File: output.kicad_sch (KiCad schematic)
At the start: 74 parts

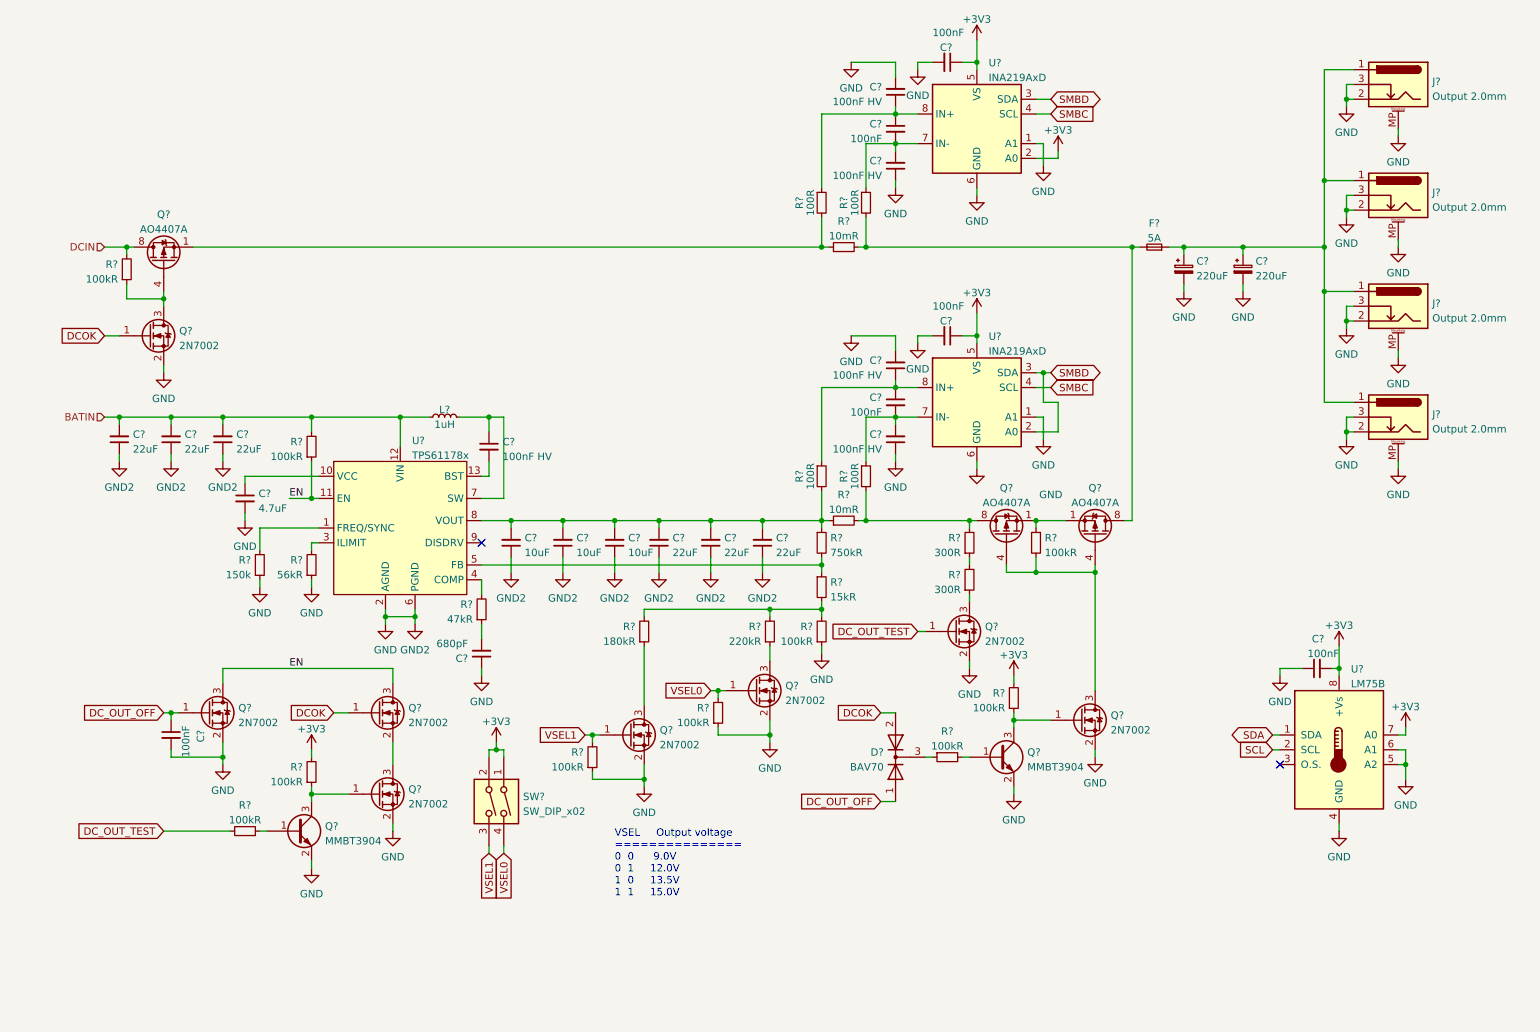
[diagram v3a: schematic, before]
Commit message: Add individually switchable outputs
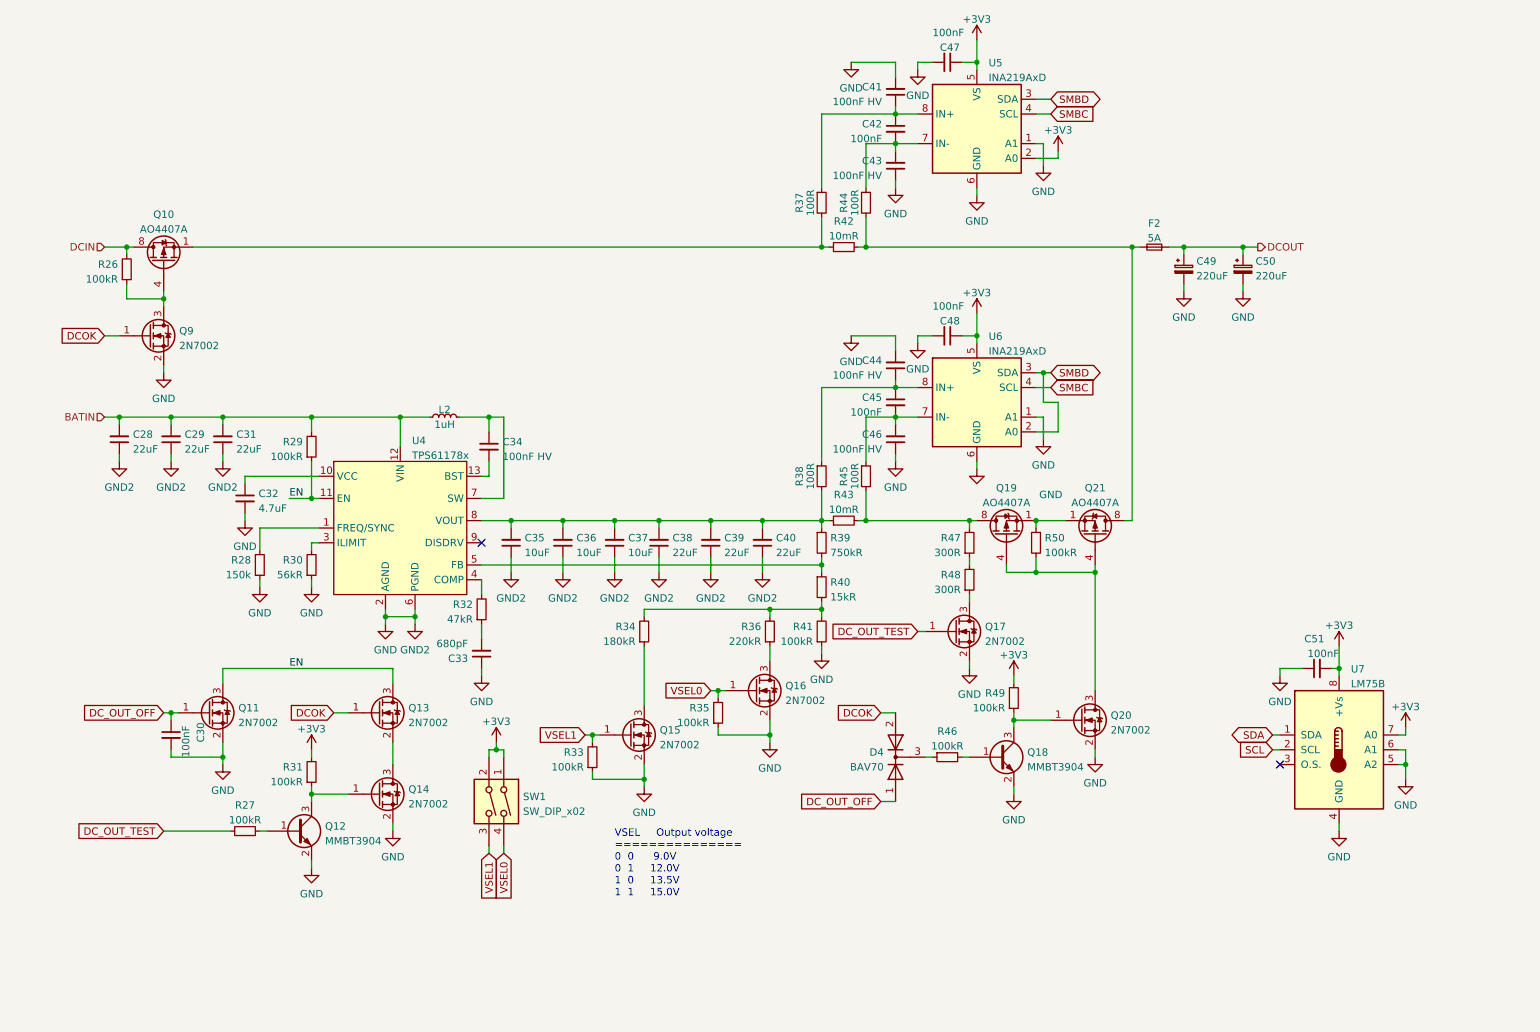
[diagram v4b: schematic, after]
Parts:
- removed J? (x4): Output 2.0mm, Connector_BarrelJack_LCSC:BarrelJack_2.0mm_DC-044B, symbol Connector:Barrel_Jack_Switch_MountingPin
- gave numbers to parts that had none: 70
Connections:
- net DCOUT: now reaches C49.1, C50.1, F2.1

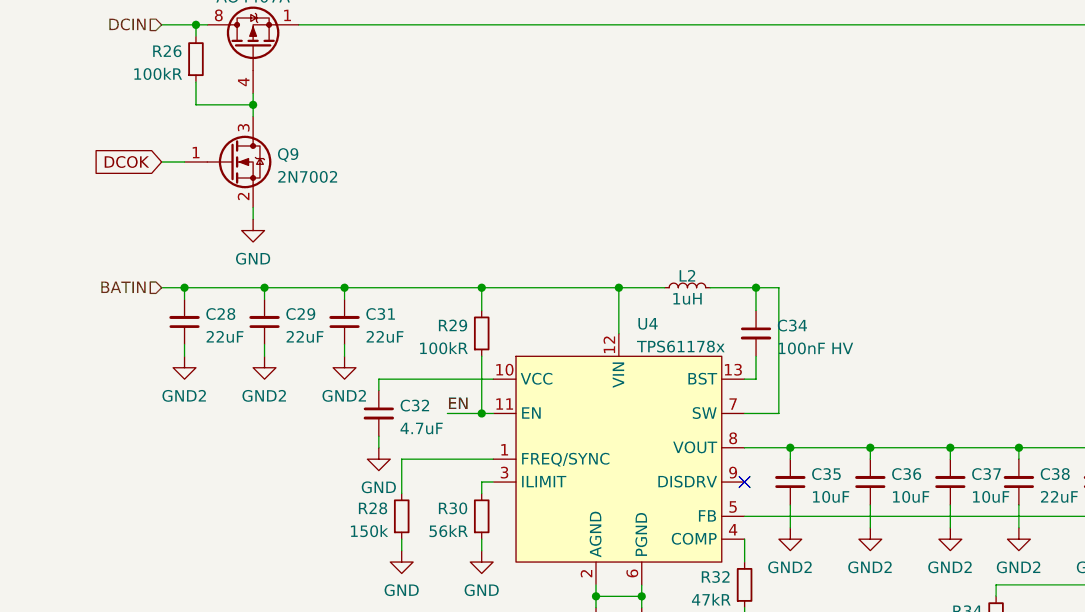
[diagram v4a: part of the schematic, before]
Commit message: Finish step-up component placement and partial layout
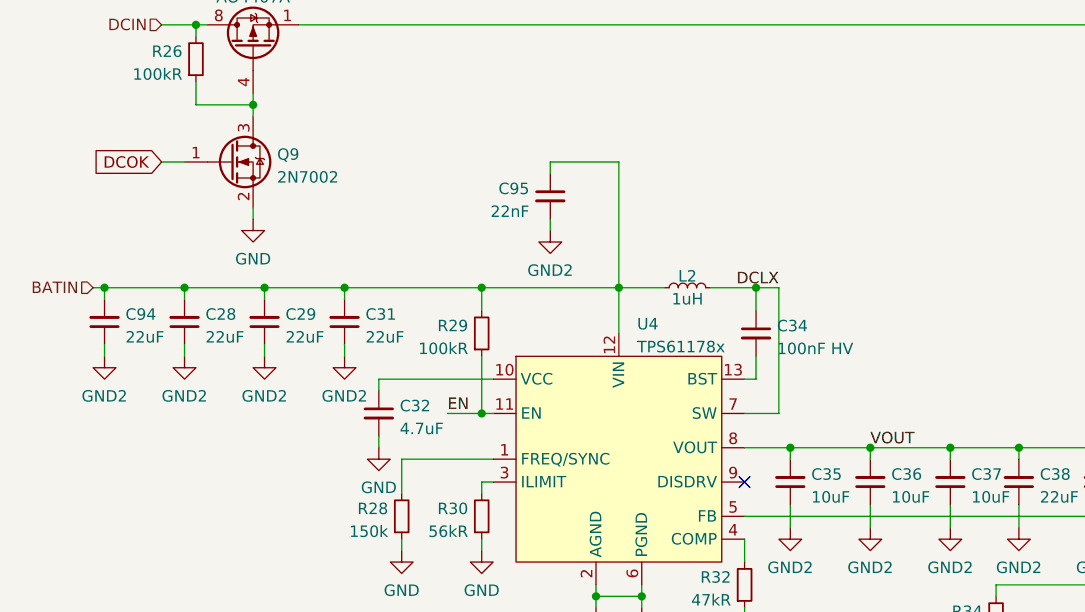
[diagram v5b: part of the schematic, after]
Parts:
- added C94: 22uF, Capacitor_SMD:C_0805_2012Metric, symbol Device:C_Small
- added C95: 22nF, Capacitor_SMD:C_0402_1005Metric, symbol Device:C_Small
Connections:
- net BATIN: now also C94.2, C95.1
- net GND: now also C94.1, C95.2
- net VOUT: now reaches C35.2, C36.2, C37.2, C38.2, C39.2, C40.2, R38.2, R39.1, R43.1, U4.8 (VOUT)
- net DCLX: now reaches C34.1, L2.2, U4.7 (SW)
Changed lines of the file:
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@@
   (junction (at 161.29 104.14) (diameter 0) (color 0 0 0 0)
+  )
+  (junction (at 31.75 86.36) (diameter 0) (color 0 0 0 0)
   )
   (junction (at 58.42 144.78) (diameter 0) (color 0 0 0 0)
@@
     (stroke (width 0) (type default) (color 0 0 0 0))
   )
+  (wire (pts (xy 31.75 86.36) (xy 40.64 86.36))
+    (stroke (width 0) (type default) (color 0 0 0 0))
+  )
   (wire (pts (xy 168.91 57.15) (xy 214.63 57.15))
     (stroke (width 0) (type default) (color 0 0 0 0))
@@
     (stroke (width 0) (type default) (color 0 0 0 0))
   )
+  (wire (pts (xy 81.28 72.39) (xy 81.28 73.66))
+    (stroke (width 0) (type default) (color 0 0 0 0))
+  )
   (wire (pts (xy 173.99 39.37) (xy 173.99 40.64))
     (stroke (width 0) (type default) (color 0 0 0 0))
@@
     (stroke (width 0) (type default) (color 0 0 0 0))
   )
-  (wire (pts (xy 38.1 86.36) (xy 40.64 86.36))
+  (wire (pts (xy 30.48 86.36) (xy 31.75 86.36))
     (stroke (width 0) (type default) (color 0 0 0 0))
   )
@@
     (stroke (width 0) (type default) (color 0 0 0 0))
   )
+  (wire (pts (xy 31.75 92.71) (xy 31.75 93.98))
+    (stroke (width 0) (type default) (color 0 0 0 0))
+  )
+  (wire (pts (xy 88.9 72.39) (xy 81.28 72.39))
+    (stroke (width 0) (type default) (color 0 0 0 0))
+  )
   (wire (pts (xy 48.26 77.47) (xy 48.26 78.74))
     (stroke (width 0) (type default) (color 0 0 0 0))
@@
     (stroke (width 0) (type default) (color 0 0 0 0))
   )
+  (wire (pts (xy 31.75 86.36) (xy 31.75 87.63))
+    (stroke (width 0) (type default) (color 0 0 0 0))
+  )
   (wire (pts (xy 62.23 96.52) (xy 62.23 97.79))
     (stroke (width 0) (type default) (color 0 0 0 0))
@@
     (stroke (width 0) (type default) (color 0 0 0 0))
   )
+  (wire (pts (xy 88.9 86.36) (xy 88.9 72.39))
+    (stroke (width 0) (type default) (color 0 0 0 0))
+  )
   (wire (pts (xy 186.69 116.84) (xy 186.69 118.11))
     (stroke (width 0) (type default) (color 0 0 0 0))
@@
   )
   (wire (pts (xy 194.31 138.43) (xy 194.31 139.7))
+    (stroke (width 0) (type default) (color 0 0 0 0))
+  )
+  (wire (pts (xy 81.28 78.74) (xy 81.28 80.01))
     (stroke (width 0) (type default) (color 0 0 0 0))
   )
@@
     (effects (font (size 1.27 1.27)) (justify left bottom))
   )
+  (label "DCLX" (at 106.68 86.36 180)
+    (effects (font (size 1.27 1.27)) (justify right bottom))
+  )
   (label "EN" (at 69.85 129.54 0)
+    (effects (font (size 1.27 1.27)) (justify left bottom))
+  )
+  (label "VOUT" (at 116.84 104.14 0)
     (effects (font (size 1.27 1.27)) (justify left bottom))
   )
@@
     (effects (font (size 1.27 1.27)) (justify left))
   )
-  (hierarchical_label "BATIN" (shape input) (at 38.1 86.36 180)
+  (hierarchical_label "BATIN" (shape input) (at 30.48 86.36 180)
     (effects (font (size 1.27 1.27)) (justify right))
   )
@@
     )
     (property "LCSC" "C25767" (id 4) (at 152.4 123.19 0)
+      (effects (font (size 1.27 1.27)) hide)
+    )
+    (pin "1")
+    (pin "2")
+  )
+  (symbol (lib_id "Device:C_Small") (at 81.28 76.2 0) (mirror y) (unit 1)
+    (in_bom yes) (on_board yes)
+    (property "Reference" "C95" (id 0) (at 78.9559 75.3716 0)
+      (effects (font (size 1.27 1.27)) (justify left))
+    )
+    (property "Value" "22nF" (id 1) (at 78.9559 77.9085 0)
+      (effects (font (size 1.27 1.27)) (justify left))
+    )
+    (property "Footprint" "Capacitor_SMD:C_0402_1005Metric" (id 2) (at 81.28 76.2 0)
+      (effects (font (size 1.27 1.27)) hide)
+    )
+    (property "Datasheet" "~" (id 3) (at 81.28 76.2 0)
+      (effects (font (size 1.27 1.27)) hide)
+    )
+    (property "LCSC" "C1532" (id 4) (at 81.28 76.2 0)
       (effects (font (size 1.27 1.27)) hide)
     )
@@
     (pin "2")
   )
+  (symbol (lib_id "power:GND2") (at 81.28 80.01 0) (unit 1)
+    (in_bom yes) (on_board yes) (fields_autoplaced)
+    (property "Reference" "#PWR0285" (id 0) (at 81.28 86.36 0)
+      (effects (font (size 1.27 1.27)) hide)
+    )
+    (property "Value" "GND2" (id 1) (at 81.28 84.4534 0))
+    (property "Footprint" "" (id 2) (at 81.28 80.01 0)
+      (effects (font (size 1.27 1.27)) hide)
+    )
+    (property "Datasheet" "" (id 3) (at 81.28 80.01 0)
+      (effects (font (size 1.27 1.27)) hide)
+    )
+    (pin "1")
+  )
   (symbol (lib_id "power:+3V3") (at 250.19 125.73 0) (unit 1)
     (in_bom yes) (on_board yes) (fields_autoplaced)
@@
     )
     (property "LCSC" "C25755" (id 4) (at 64.77 111.76 0)
+      (effects (font (size 1.27 1.27)) hide)
+    )
+    (pin "1")
+    (pin "2")
+  )
+  (symbol (lib_id "Device:C_Small") (at 31.75 90.17 180) (unit 1)
+    (in_bom yes) (on_board yes) (fields_autoplaced)
+    (property "Reference" "C94" (id 0) (at 34.0741 89.3289 0)
+      (effects (font (size 1.27 1.27)) (justify right))
+    )
+    (property "Value" "22uF" (id 1) (at 34.0741 91.8658 0)
+      (effects (font (size 1.27 1.27)) (justify right))
+    )
+    (property "Footprint" "Capacitor_SMD:C_0805_2012Metric" (id 2) (at 31.75 90.17 0)
+      (effects (font (size 1.27 1.27)) hide)
+    )
+    (property "Datasheet" "~" (id 3) (at 31.75 90.17 0)
+      (effects (font (size 1.27 1.27)) hide)
+    )
+    (property "LCSC" "C45783" (id 4) (at 31.75 90.17 0)
       (effects (font (size 1.27 1.27)) hide)
     )
@@
       (effects (font (size 1.27 1.27)) hide)
     )
+    (pin "1")
+  )
+  (symbol (lib_id "power:GND2") (at 31.75 93.98 0) (unit 1)
+    (in_bom yes) (on_board yes) (fields_autoplaced)
+    (property "Reference" "#PWR0284" (id 0) (at 31.75 100.33 0)
+      (effects (font (size 1.27 1.27)) hide)
+    )
+    (property "Value" "GND2" (id 1) (at 31.75 98.4234 0))
+    (property "Footprint" "" (id 2) (at 31.75 93.98 0)
+      (effects (font (size 1.27 1.27)) hide)
+    )
+    (property "Datasheet" "" (id 3) (at 31.75 93.98 0)
+      (effects (font (size 1.27 1.27)) hide)
+    )

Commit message: Finish initial layout
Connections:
- net DCOK: now also D4.1 (A); no longer D4.2 (A)
- net DC_OUT_OFF: now also D4.2 (A); no longer D4.1 (A)
- net DCBUS: now reaches F2.2, Q21.5 (D), Q21.6 (D), Q21.7 (D), Q21.8 (D), R42.2, R44.2
- net DCTHRU: now reaches Q10.1 (S), Q10.2 (S), Q10.3 (S), R37.2, R42.1
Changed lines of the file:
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@@
+    (effects (font (size 1.27 1.27)) (justify left bottom))
+  )
+  (label "DCBUS" (at 207.01 57.15 0)
     (effects (font (size 1.27 1.27)) (justify left bottom))
   )
@@
   )
   (label "VOUT" (at 116.84 104.14 0)
+    (effects (font (size 1.27 1.27)) (justify left bottom))
+  )
+  (label "DCTHRU" (at 152.4 57.15 0)
     (effects (font (size 1.27 1.27)) (justify left bottom))
   )
@@
     (pin "2")
   )
-  (symbol (lib_id "Diode:BAV70") (at 173.99 144.78 90) (unit 1)
+  (symbol (lib_id "Diode:BAV70") (at 173.99 144.78 90) (mirror x) (unit 1)
     (in_bom yes) (on_board yes) (fields_autoplaced)
     (property "Reference" "D4" (id 0) (at 171.958 143.9453 90)

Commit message: Optimize power routing
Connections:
- net THERML: now reaches Q17.3 (D), R48.1
- net THERMM: now reaches R47.1, R48.2
- net VBUS: now reaches Q19.5 (D), Q19.6 (D), Q19.7 (D), Q19.8 (D), R43.2, R45.2, R47.2
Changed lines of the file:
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@@
     (effects (font (size 1.27 1.27)) (justify left bottom))
+  )
+  (label "THERMM" (at 186.69 111.76 180)
+    (effects (font (size 1.27 1.27)) (justify right bottom))
   )
   (label "EN" (at 69.85 100.33 0)
@@
     (effects (font (size 1.27 1.27)) (justify left bottom))
   )
+  (label "THERML" (at 186.69 118.11 0)
+    (effects (font (size 1.27 1.27)) (justify left bottom))
+  )
   (label "DCLX" (at 106.68 86.36 180)
     (effects (font (size 1.27 1.27)) (justify right bottom))
   )
+  (label "VBUS" (at 175.26 104.14 0)
+    (effects (font (size 1.27 1.27)) (justify left bottom))
+  )
   (label "EN" (at 69.85 129.54 0)

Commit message: Fix footprint origins for JLC assembly
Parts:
- C28, C29, C31, C38, C39, C40, C94: LCSC C45783 -> C602037
- Q10, Q19, Q21: LCSC C16072 -> C35349
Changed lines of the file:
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@@
       (effects (font (size 1.27 1.27)) hide)
     )
-    (property "LCSC" "C45783" (id 4) (at 40.64 90.17 0)
+    (property "LCSC" "C602037" (id 4) (at 40.64 90.17 0)
       (effects (font (size 1.27 1.27)) hide)
     )
@@
       (effects (font (size 1.27 1.27)) hide)
     )
-    (property "LCSC" "C45783" (id 4) (at 31.75 90.17 0)
+    (property "LCSC" "C602037" (id 4) (at 31.75 90.17 0)
       (effects (font (size 1.27 1.27)) hide)
     )
@@
       (effects (font (size 1.27 1.27)) hide)
     )
-    (property "LCSC" "C45783" (id 4) (at 133.35 107.95 0)
+    (property "LCSC" "C602037" (id 4) (at 133.35 107.95 0)
       (effects (font (size 1.27 1.27)) hide)
     )
@@
       (effects (font (size 1.27 1.27)) hide)
     )
-    (property "LCSC" "C45783" (id 4) (at 49.53 90.17 0)
+    (property "LCSC" "C602037" (id 4) (at 49.53 90.17 0)
       (effects (font (size 1.27 1.27)) hide)
     )
@@
       (effects (font (size 1.27 1.27) italic) (justify left) hide)
     )
-    (property "Datasheet" "https://datasheet.lcsc.com/szlcsc/Alpha-Omega-Semicon-AOS-AO4407A_C16072.pdf" (id 3) (at 208.28 106.68 90)
+    (property "Datasheet" "https://datasheet.lcsc.com/szlcsc/Alpha-Omega-Semicon-AOS-AO4407A_C35349.pdf" (id 3) (at 208.28 106.68 90)
       (effects (font (size 1.27 1.27)) (justify left) hide)
     )
-    (property "LCSC" "C16072" (id 4) (at 208.28 106.68 0)
+    (property "LCSC" "C35349" (id 4) (at 208.28 106.68 0)
       (effects (font (size 1.27 1.27)) hide)
     )
@@
       (effects (font (size 1.27 1.27) italic) (justify left) hide)
     )
-    (property "Datasheet" "https://datasheet.lcsc.com/szlcsc/Alpha-Omega-Semicon-AOS-AO4407A_C16072.pdf" (id 3) (at 48.26 59.69 90)
+    (property "Datasheet" "https://datasheet.lcsc.com/szlcsc/Alpha-Omega-Semicon-AOS-AO4407A_C35349.pdf" (id 3) (at 48.26 59.69 90)
       (effects (font (size 1.27 1.27)) (justify left) hide)
     )
-    (property "LCSC" "C16072" (id 4) (at 48.26 59.69 0)
+    (property "LCSC" "C35349" (id 4) (at 48.26 59.69 0)
       (effects (font (size 1.27 1.27)) hide)
     )
@@
       (effects (font (size 1.27 1.27) italic) (justify left) hide)
     )
-    (property "Datasheet" "https://datasheet.lcsc.com/szlcsc/Alpha-Omega-Semicon-AOS-AO4407A_C16072.pdf" (id 3) (at 193.04 106.68 90)
+    (property "Datasheet" "https://datasheet.lcsc.com/szlcsc/Alpha-Omega-Semicon-AOS-AO4407A_C35349.pdf" (id 3) (at 193.04 106.68 90)
       (effects (font (size 1.27 1.27)) (justify left) hide)
     )
-    (property "LCSC" "C16072" (id 4) (at 193.04 106.68 0)
+    (property "LCSC" "C35349" (id 4) (at 193.04 106.68 0)
       (effects (font (size 1.27 1.27)) hide)
     )
@@
       (effects (font (size 1.27 1.27)) hide)
     )
-    (property "LCSC" "C45783" (id 4) (at 151.13 107.95 0)
+    (property "LCSC" "C602037" (id 4) (at 151.13 107.95 0)
       (effects (font (size 1.27 1.27)) hide)
     )
@@
       (effects (font (size 1.27 1.27)) hide)
     )
-    (property "LCSC" "C45783" (id 4) (at 142.24 107.95 0)
+    (property "LCSC" "C602037" (id 4) (at 142.24 107.95 0)
       (effects (font (size 1.27 1.27)) hide)
     )
@@
       (effects (font (size 1.27 1.27)) hide)
     )
-    (property "LCSC" "C45783" (id 4) (at 58.42 90.17 0)
-      (effects (font (size 1.27 1.27)) hide)
-    )
+    (property "LCSC" "C602037" (id 4) (at 58.42 90.17 0)
+      (effects (font (size 1.27 1.27)) hide)
+    )
